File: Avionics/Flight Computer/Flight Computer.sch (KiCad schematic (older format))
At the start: 2 parts

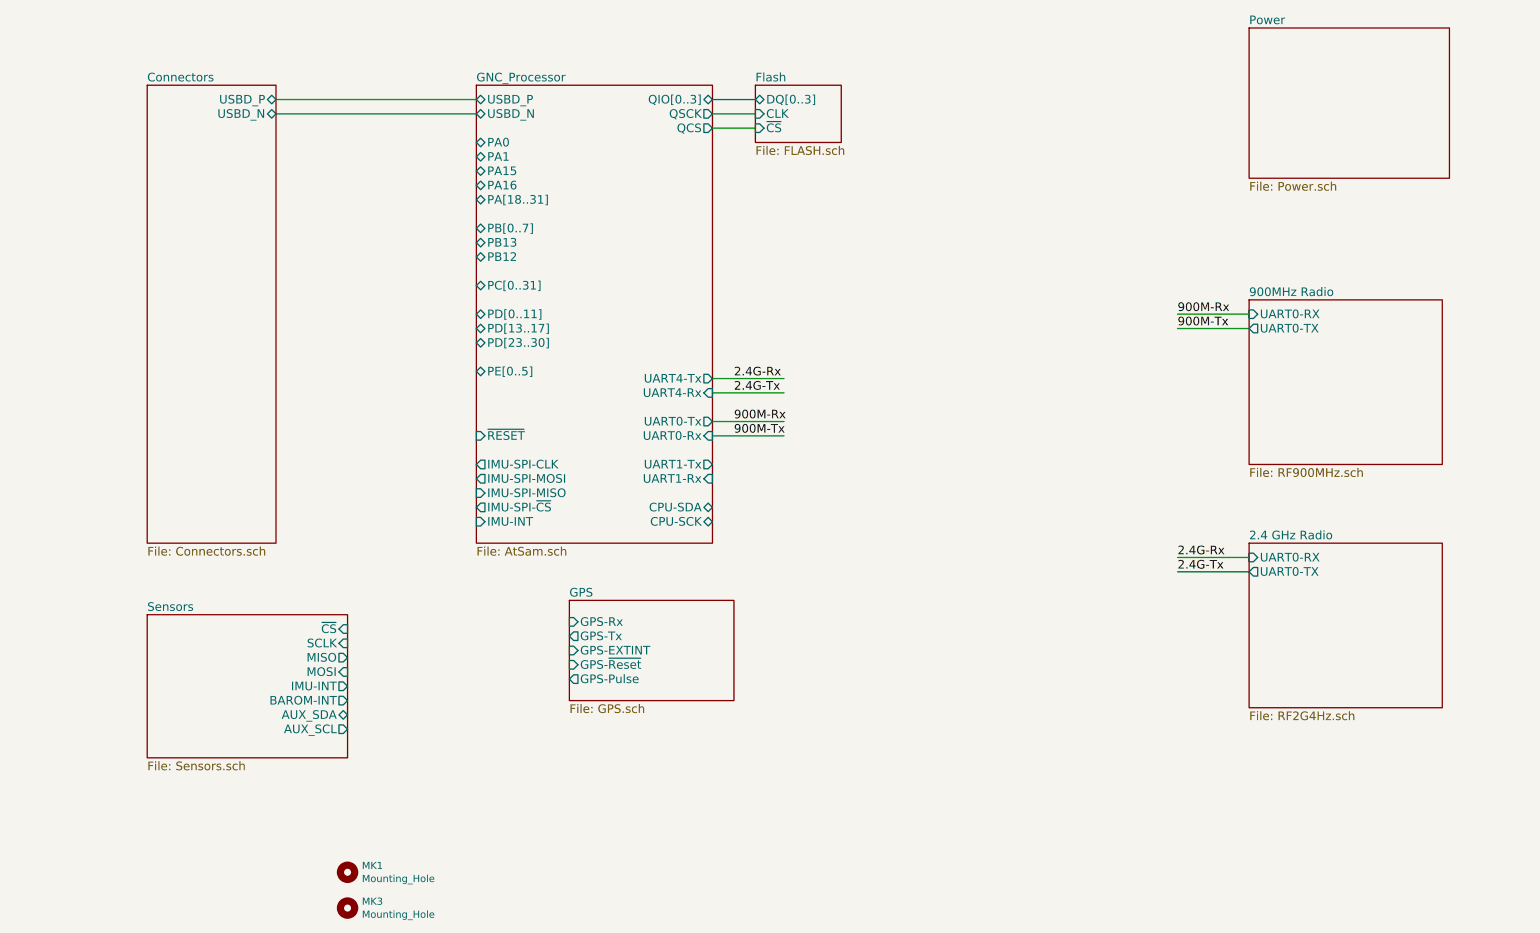
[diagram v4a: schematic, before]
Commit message: Wired up everything and started rearranging layout
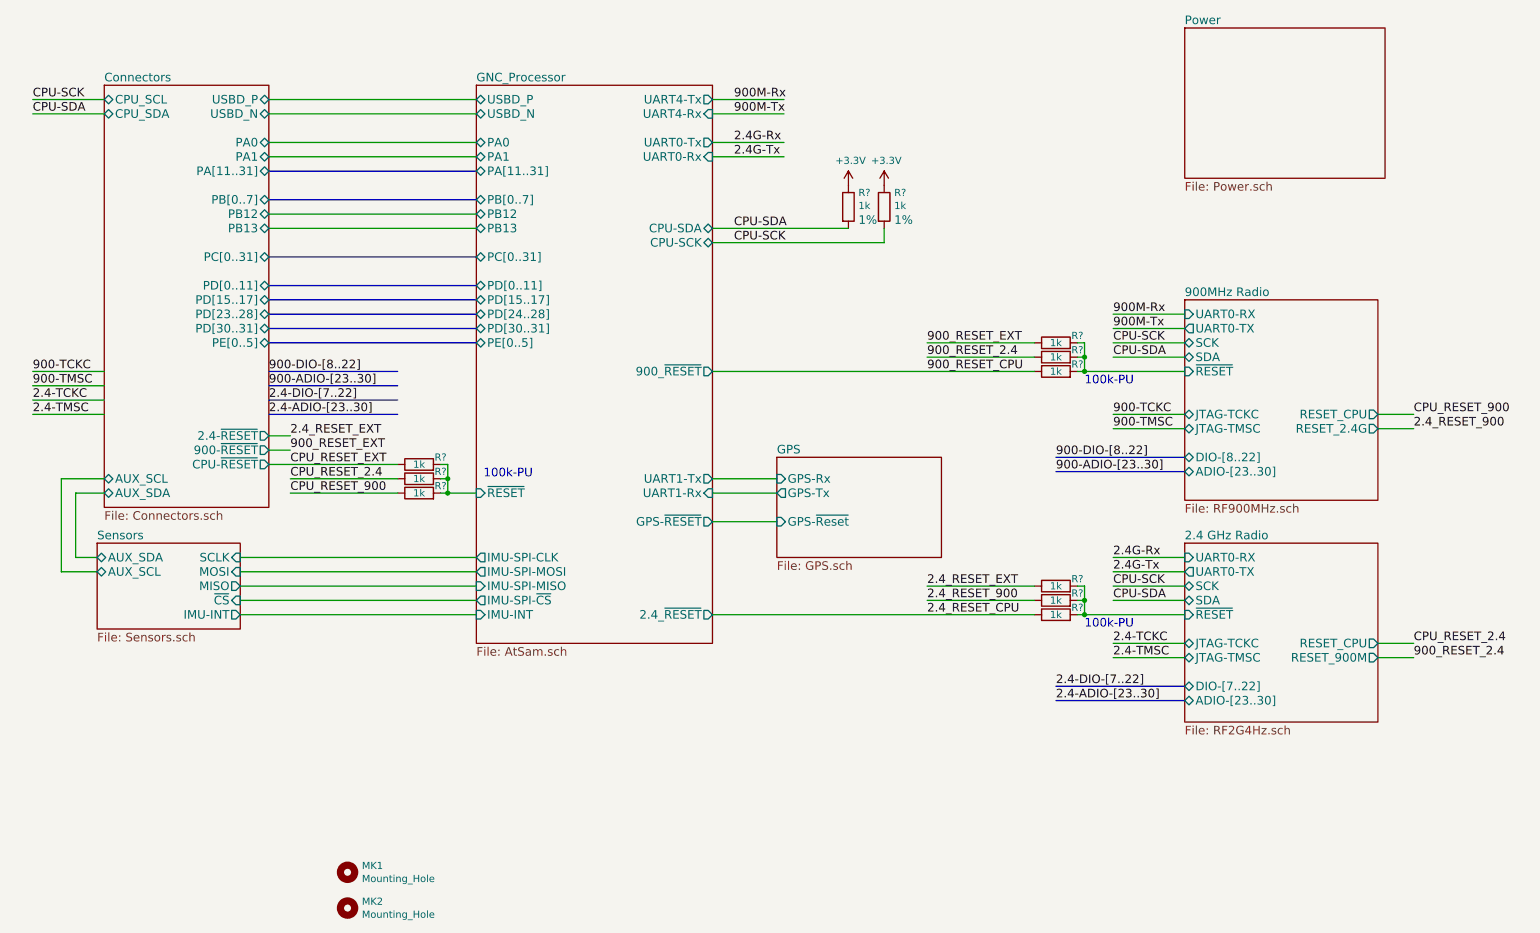
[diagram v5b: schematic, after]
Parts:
- added R? (x11): 1k, Resistors_SMD:R_0402, symbol R
- renumbered MK3 to MK2
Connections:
- net labels added: +3.3V, 2.4-ADIO-[23..30], 2.4-DIO-[7..22], 2.4-TCKC, 2.4-TMSC, 2.4_RESET_900, 2.4_RESET_CPU, 2.4_RESET_EXT, 900-ADIO-[23..30], 900-DIO-[8..22], 900-TCKC, 900-TMSC, 900_RESET_2.4, 900_RESET_CPU, 900_RESET_EXT, CPU-SCK, CPU-SDA, CPU_RESET_2.4, CPU_RESET_900, CPU_RESET_EXT
- wire segments 12 -> 72
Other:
- note added: "100k-PU"

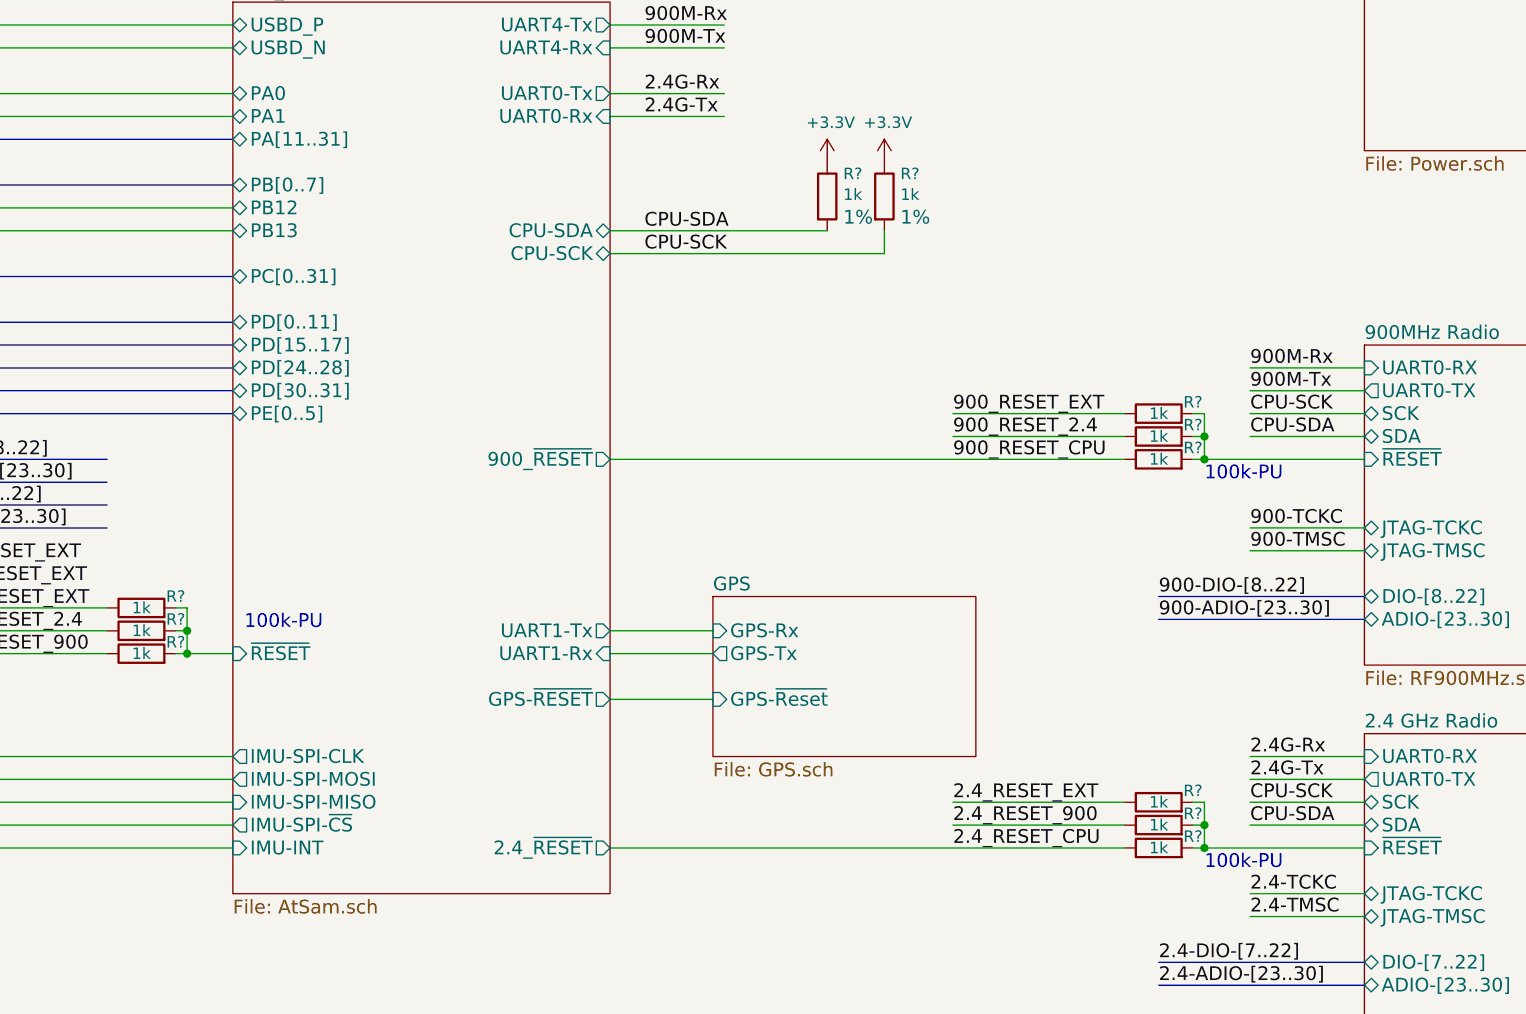
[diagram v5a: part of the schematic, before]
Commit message: Finished breaking out signals to connector sheet and interconnecting processors.
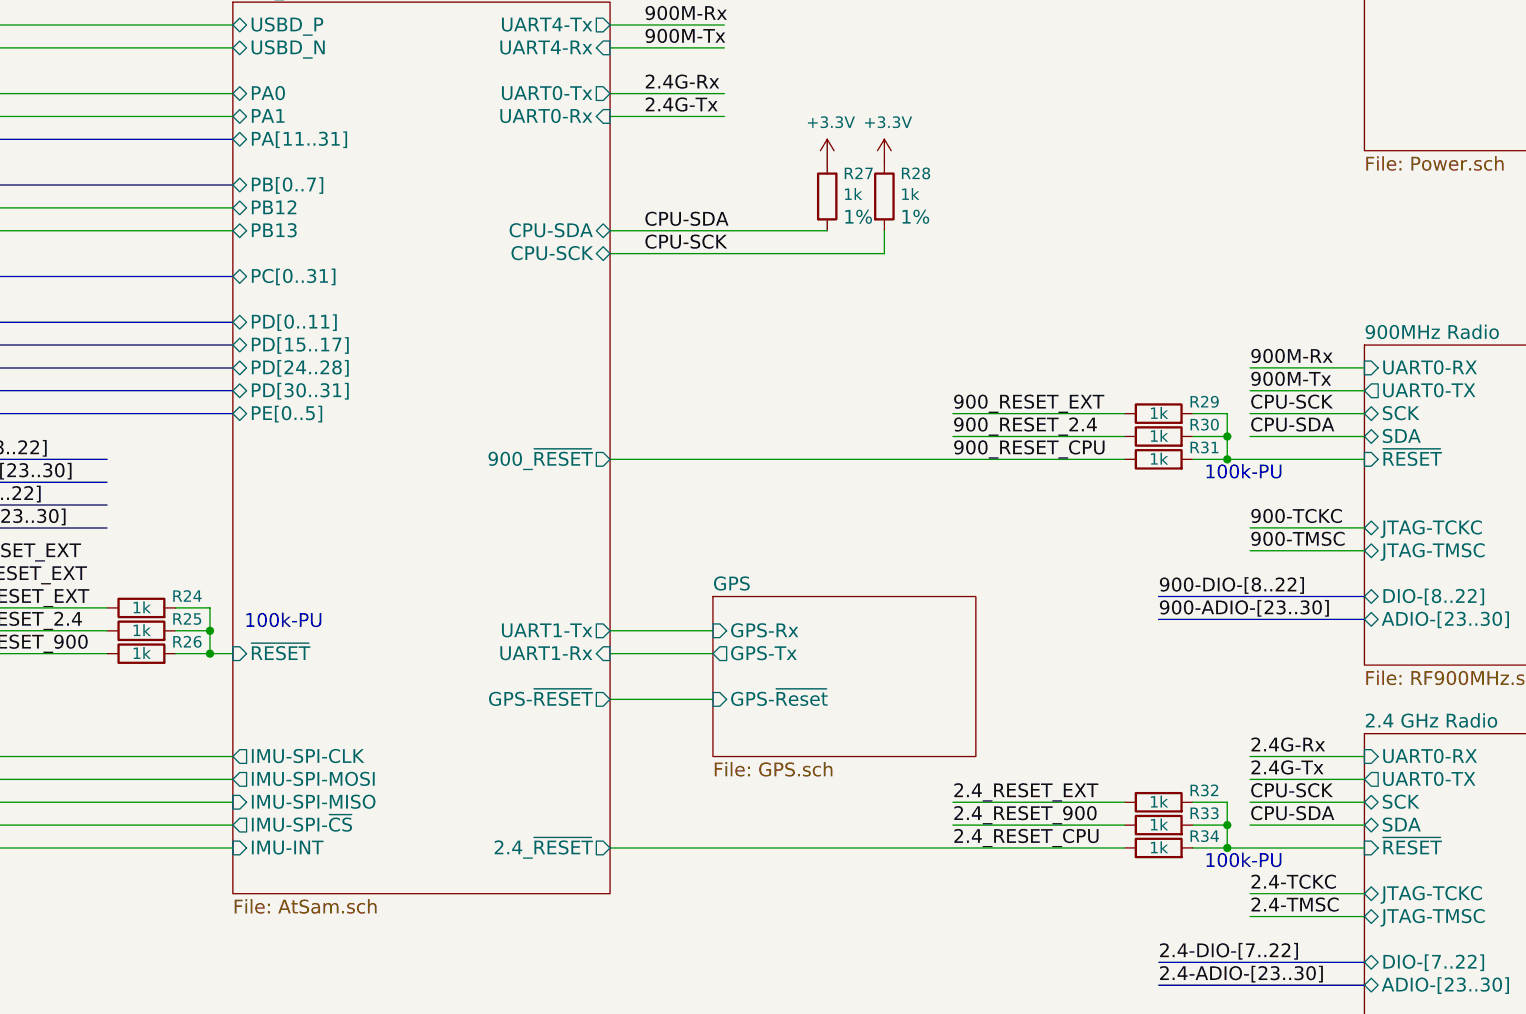
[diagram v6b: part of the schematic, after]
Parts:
- gave numbers to parts that had none: 11
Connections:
- wire segments 72 -> 78
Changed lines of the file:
@@
 CPU-SDA
 $Comp
-L R R?
+L R R27
 U 1 1 58BFD165
 P 6400 2350
-F 0 "R?" H 6470 2449 50  0000 L CNN
+F 0 "R27" H 6470 2449 50  0000 L CNN
 F 1 "1k" H 6470 2358 50  0000 L CNN
 F 2 "Resistors_SMD:R_0402" V -1050 700 50  0001 C CNN
@@
 $EndComp
 $Comp
-L R R?
+L R R28
 U 1 1 58BFD565
 P 6650 2350
-F 0 "R?" H 6720 2449 50  0000 L CNN
+F 0 "R28" H 6720 2449 50  0000 L CNN
 F 1 "1k" H 6720 2358 50  0000 L CNN
 F 2 "Resistors_SMD:R_0402" V -800 700 50  0001 C CNN
@@
 $EndComp
 $Comp
-L +3.3V #PWR?
+L +3.3V #PWR01
 U 1 1 58BFF81C
 P 6650 2200
-F 0 "#PWR?" H 4950 -300 50  0001 C CNN
+F 0 "#PWR01" H 4950 -300 50  0001 C CNN
 F 1 "+3.3V" H 6665 2373 50  0000 C CNN
 F 2 "" H 4950 -150 50  0001 C CNN
@@
 $EndComp
 $Comp
-L +3.3V #PWR?
+L +3.3V #PWR02
 U 1 1 58BFF8E0
 P 6400 2200
-F 0 "#PWR?" H 4700 -300 50  0001 C CNN
+F 0 "#PWR02" H 4700 -300 50  0001 C CNN
 F 1 "+3.3V" H 6415 2373 50  0000 C CNN
 F 2 "" H 4700 -150 50  0001 C CNN
@@
 $EndComp
 $Comp
-L R R?
+L R R26
 U 1 1 58C0DD41
 P 3400 4350
-F 0 "R?" V 3450 4200 50  0000 C CNN
+F 0 "R26" V 3450 4150 50  0000 C CNN
 F 1 "1k" V 3400 4350 50  0000 C CNN
 F 2 "Resistors_SMD:R_0402" V -4050 2700 50  0001 C CNN
@@
 $EndComp
 $Comp
-L R R?
+L R R25
 U 1 1 58C11226
 P 3400 4250
-F 0 "R?" V 3450 4100 50  0000 C CNN
+F 0 "R25" V 3450 4050 50  0000 C CNN
 F 1 "1k" V 3400 4250 50  0000 C CNN
 F 2 "Resistors_SMD:R_0402" V -4050 2600 50  0001 C CNN
@@
 $EndComp
 $Comp
-L R R?
+L R R24
 U 1 1 58C113C8
 P 3400 4150
-F 0 "R?" V 3450 4000 50  0000 C CNN
+F 0 "R24" V 3450 3950 50  0000 C CNN
 F 1 "1k" V 3400 4150 50  0000 C CNN
 F 2 "Resistors_SMD:R_0402" V -4050 2500 50  0001 C CNN
@@
 100k-PU
 $Comp
-L R R?
+L R R34
 U 1 1 58C4A4F7
 P 7850 5200
-F 0 "R?" V 7900 5050 50  0000 C CNN
+F 0 "R34" V 7900 5000 50  0000 C CNN
 F 1 "1k" V 7850 5200 50  0000 C CNN
 F 2 "Resistors_SMD:R_0402" V 400 3550 50  0001 C CNN
@@
 $EndComp
 $Comp
-L R R?
+L R R33
 U 1 1 58C4A502
 P 7850 5100
-F 0 "R?" V 7900 4950 50  0000 C CNN
+F 0 "R33" V 7900 4900 50  0000 C CNN
 F 1 "1k" V 7850 5100 50  0000 C CNN
 F 2 "Resistors_SMD:R_0402" V 400 3450 50  0001 C CNN
@@
 $EndComp
 $Comp
-L R R?
+L R R32
 U 1 1 58C4A50D
 P 7850 5000
-F 0 "R?" V 7900 4850 50  0000 C CNN
+F 0 "R32" V 7900 4800 50  0000 C CNN
 F 1 "1k" V 7850 5000 50  0000 C CNN
 F 2 "Resistors_SMD:R_0402" V 400 3350 50  0001 C CNN
@@
 100k-PU
 $Comp
-L R R?
+L R R31
 U 1 1 58C89A2C
 P 7850 3500
-F 0 "R?" V 7900 3350 50  0000 C CNN
+F 0 "R31" V 7900 3300 50  0000 C CNN
 F 1 "1k" V 7850 3500 50  0000 C CNN
 F 2 "Resistors_SMD:R_0402" V 400 1850 50  0001 C CNN
@@
 $EndComp
 $Comp
-L R R?
+L R R30
 U 1 1 58C89A37
 P 7850 3400
-F 0 "R?" V 7900 3250 50  0000 C CNN
+F 0 "R30" V 7900 3200 50  0000 C CNN
 F 1 "1k" V 7850 3400 50  0000 C CNN
 F 2 "Resistors_SMD:R_0402" V 400 1750 50  0001 C CNN
@@
 $EndComp
 $Comp
-L R R?
+L R R29
 U 1 1 58C89A42
 P 7850 3300
-F 0 "R?" V 7900 3150 50  0000 C CNN
+F 0 "R29" V 7900 3100 50  0000 C CNN
 F 1 "1k" V 7850 3300 50  0000 C CNN
 F 2 "Resistors_SMD:R_0402" V 400 1650 50  0001 C CNN
@@
 	6650 2600 6650 2500
 Wire Wire Line
-	3550 4350 3800 4350
-Wire Wire Line
-	3550 4250 3600 4250
-Wire Wire Line
-	3600 4150 3600 4350
-Connection ~ 3600 4350
-Wire Wire Line
-	3600 4150 3550 4150
-Connection ~ 3600 4250
+	3550 4350 3700 4350
+Wire Wire Line
+	3700 4350 3800 4350
+Wire Wire Line
+	3550 4250 3700 4250
+Wire Wire Line
+	3700 4150 3700 4250
+Wire Wire Line
+	3700 4250 3700 4350
+Connection ~ 3700 4350
+Wire Wire Line
+	3700 4150 3550 4150
+Connection ~ 3700 4250
 Wire Wire Line
 	2350 4150 3250 4150
@@
 	10100 5500 10350 5500
 Wire Wire Line
-	8000 5200 8750 5200
-Wire Wire Line
-	8000 5100 8050 5100
-Wire Wire Line
-	8050 5000 8050 5200
-Connection ~ 8050 5200
-Wire Wire Line
-	8050 5000 8000 5000
-Connection ~ 8050 5100
+	8000 5200 8150 5200
+Wire Wire Line
+	8150 5200 8750 5200
+Wire Wire Line
+	8000 5100 8150 5100
+Wire Wire Line
+	8150 5000 8150 5100
+Wire Wire Line
+	8150 5100 8150 5200
+Connection ~ 8150 5200
+Wire Wire Line
+	8150 5000 8000 5000
+Connection ~ 8150 5100
 Wire Wire Line
 	7700 5000 6950 5000
@@
 	7850 4200 8750 4200
 Wire Wire Line
-	8000 3500 8750 3500
-Wire Wire Line
-	8000 3400 8050 3400
-Wire Wire Line
-	8050 3300 8050 3500
-Connection ~ 8050 3500
-Wire Wire Line
-	8050 3300 8000 3300
-Connection ~ 8050 3400
+	8000 3500 8150 3500
+Wire Wire Line
+	8150 3500 8750 3500
+Wire Wire Line
+	8000 3400 8150 3400
+Wire Wire Line
+	8150 3300 8150 3400
+Wire Wire Line
+	8150 3400 8150 3500
+Connection ~ 8150 3500
+Wire Wire Line
+	8150 3300 8000 3300
+Connection ~ 8150 3400
 Wire Wire Line
 	7700 3300 6950 3300
